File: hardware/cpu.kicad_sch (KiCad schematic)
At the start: 5 parts, among them U3 ESP32-C3-WROOM-02

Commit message: Update.
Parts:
- removed Conn_02x1: Conn_02x05_Odd_Even, Connector_PinHeader_2.54mm:PinHeader_2x05_P2.54mm_Vertical, symbol Connector_Generic:Conn_02x05_Odd_Even
- added J3: Conn_02x04_Odd_Even, Connector_PinHeader_2.54mm:PinHeader_2x04_P2.54mm_Vertical, symbol Connector_Generic:Conn_02x04_Odd_Even
- renumbered D3 to D4, R15 to R4, R6 to R5
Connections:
- net GND: now also J3.5 (Pin_5), J3.7 (Pin_7)
- net at U3.12 (IO21/TXD): now also J3.1 (Pin_1)
- net at U3.11 (IO20/RXD): now also J3.2 (Pin_2)
- net at U3.4 (IO5): now also J3.3 (Pin_3)
- net at U3.17 (IO1): now also J3.4 (Pin_4)
- net at U3.15 (IO3): now also J3.6 (Pin_6)
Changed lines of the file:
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@@
+	)
+	(junction
+		(at 36.83 58.42)
+		(diameter 0)
+		(color 0 0 0 0)
 	)
 	(junction
@@
 	(wire
 		(pts
-			(xy 34.29 58.42) (xy 36.83 58.42)
-		)
-		(stroke
-			(width 0)
-			(type default)
-		)
-	)
-	(wire
-		(pts
 			(xy 49.53 53.34) (xy 54.61 53.34)
 		)
@@
 	(wire
 		(pts
-			(xy 49.53 58.42) (xy 52.07 58.42)
-		)
-		(stroke
-			(width 0)
-			(type default)
-		)
-	)
-	(wire
-		(pts
-			(xy 52.07 63.5) (xy 95.25 63.5)
-		)
-		(stroke
-			(width 0)
-			(type default)
-		)
-	)
-	(wire
-		(pts
 			(xy 92.71 41.91) (xy 92.71 48.26)
 		)
@@
 	(wire
 		(pts
-			(xy 95.25 78.74) (xy 34.29 78.74)
-		)
-		(stroke
-			(width 0)
-			(type default)
-		)
-	)
-	(wire
-		(pts
-			(xy 34.29 78.74) (xy 34.29 58.42)
+			(xy 36.83 55.88) (xy 36.83 58.42)
 		)
 		(stroke
@@
 	(wire
 		(pts
-			(xy 95.25 71.12) (xy 33.02 71.12)
-		)
-		(stroke
-			(width 0)
-			(type default)
-		)
-	)
-	(wire
-		(pts
 			(xy 104.14 38.1) (xy 110.49 38.1)
 		)
@@
 	(wire
 		(pts
+			(xy 36.83 58.42) (xy 36.83 60.96)
+		)
+		(stroke
+			(width 0)
+			(type default)
+		)
+	)
+	(wire
+		(pts
 			(xy 76.2 38.1) (xy 104.14 38.1)
 		)
@@
 	(wire
 		(pts
-			(xy 33.02 71.12) (xy 33.02 55.88)
-		)
-		(stroke
-			(width 0)
-			(type default)
-		)
-	)
-	(wire
-		(pts
 			(xy 36.83 53.34) (xy 31.75 53.34)
 		)
@@
 		(pts
 			(xy 110.49 38.1) (xy 110.49 43.18)
-		)
-		(stroke
-			(width 0)
-			(type default)
-		)
-	)
-	(wire
-		(pts
-			(xy 52.07 63.5) (xy 52.07 58.42)
-		)
-		(stroke
-			(width 0)
-			(type default)
-		)
-	)
-	(wire
-		(pts
-			(xy 33.02 55.88) (xy 36.83 55.88)
 		)
 		(stroke
@@
 		(dnp no)
 		(fields_autoplaced yes)
-		(property "Reference" "R6"
+		(property "Reference" "R5"
 			(at 85.09 35.56 90)
 			(effects
@@
 			(project ""
 				(path "/90430e5f-7049-4de8-b92d-f897c4a89819/99bf9233-4f4b-4c20-a5a1-eeea9a6ff67a"
-					(reference "R6")
+					(reference "R5")
 					(unit 1)
 				)
@@
 	)
 	(symbol
-		(lib_id "Connector_Generic:Conn_02x05_Odd_Even")
-		(at 41.91 55.88 0)
+		(lib_id "Connector_Generic:Conn_02x04_Odd_Even")
+		(at 41.91 53.34 0)
 		(unit 1)
 		(exclude_from_sim no)
@@
 		(dnp no)
 		(fields_autoplaced yes)
-		(property "Reference" "Conn_02x1"
+		(property "Reference" "J3"
 			(at 43.18 44.45 0)
 			(effects
@@
 					(size 1.27 1.27)
 				)
-				(hide yes)
-			)
-		)
-		(property "Value" "Conn_02x05_Odd_Even"
+			)
+		)
+		(property "Value" "Conn_02x04_Odd_Even"
 			(at 43.18 46.99 0)
 			(effects
@@
 			)
 		)
-		(property "Footprint" "Connector_PinHeader_2.54mm:PinHeader_2x05_P2.54mm_Vertical"
-			(at 41.91 55.88 0)
+		(property "Footprint" "Connector_PinHeader_2.54mm:PinHeader_2x04_P2.54mm_Vertical"
+			(at 41.91 53.34 0)
 			(effects
 				(font
@@
 		)
 		(property "Datasheet" "~"
-			(at 41.91 55.88 0)
-			(effects
-				(font
-					(size 1.27 1.27)
-				)
-				(hide yes)
-			)
-		)
-		(property "Description" "Generic connector, double row, 02x05, odd/even pin numbering scheme (row 1 odd numbers, row 2 even numbers), script generated (kicad-library-utils/schlib/autogen/connector/)"
-			(at 41.91 55.88 0)
-			(effects
-				(font
-					(size 1.27 1.27)
-				)
-				(hide yes)
-			)
+			(at 41.91 53.34 0)
+			(effects
+				(font
+					(size 1.27 1.27)
+				)
+				(hide yes)
+			)
+		)
+		(property "Description" "Generic connector, double row, 02x04, odd/even pin numbering scheme (row 1 odd numbers, row 2 even numbers), script generated (kicad-library-utils/schlib/autogen/connector/)"
+			(at 41.91 53.34 0)
+			(effects
+				(font
+					(size 1.27 1.27)
+				)
+				(hide yes)
+			)
+		)
+		(pin "3"
+		)
+		(pin "8"
+		)
+		(pin "1"
 		)
 		(pin "5"
 		)
+		(pin "7"
+		)
+		(pin "2"
+		)
+		(pin "4"
+		)
 		(pin "6"
 		)
-		(pin "2"
-		)
-		(pin "7"
-		)
-		(pin "10"
-		)
-		(pin "9"
-		)
-		(pin "8"
-		)
-		(pin "4"
-		)
-		(pin "1"
-		)
-		(pin "3"
-		)
 		(instances
-			(project ""
+			(project "nixie_clock"
 				(path "/90430e5f-7049-4de8-b92d-f897c4a89819/99bf9233-4f4b-4c20-a5a1-eeea9a6ff67a"
-					(reference "Conn_02x1")
+					(reference "J3")
 					(unit 1)
 				)
@@
 		(on_board yes)
 		(dnp no)
-		(property "Reference" "D3"
+		(property "Reference" "D4"
 			(at 87.3125 46.99 0)
 			(effects
@@
 			(project ""
 				(path "/90430e5f-7049-4de8-b92d-f897c4a89819/99bf9233-4f4b-4c20-a5a1-eeea9a6ff67a"
-					(reference "D3")
+					(reference "D4")
 					(unit 1)
 				)
@@
 		(dnp no)
 		(fields_autoplaced yes)
-		(property "Reference" "R15"
+		(property "Reference" "R4"
 			(at 80.01 46.99 90)
 			(effects
@@
 			(project ""
 				(path "/90430e5f-7049-4de8-b92d-f897c4a89819/99bf9233-4f4b-4c20-a5a1-eeea9a6ff67a"
-					(reference "R15")
+					(reference "R4")
 					(unit 1)
 				)

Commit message: First routage.
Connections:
- net GND: no longer J3.5 (Pin_5), J3.7 (Pin_7)
- net at J3.1 (Pin_1): now also U3.11 (IO20/RXD); no longer U3.12 (IO21/TXD)
- net at J3.2 (Pin_2): now also U3.12 (IO21/TXD); no longer U3.11 (IO20/RXD)
- net at J3.3 (Pin_3): no longer U3.4 (IO5)
- net at J3.4 (Pin_4): no longer U3.17 (IO1)
- net at J3.6 (Pin_6): no longer U3.15 (IO3)
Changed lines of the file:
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@@
-	)
-	(junction
-		(at 36.83 58.42)
-		(diameter 0)
-		(color 0 0 0 0)
 	)
 	(junction
@@
 	(wire
 		(pts
-			(xy 53.34 60.96) (xy 95.25 60.96)
+			(xy 50.8 29.21) (xy 50.8 50.8)
 		)
 		(stroke
@@
 	(wire
 		(pts
-			(xy 49.53 53.34) (xy 54.61 53.34)
-		)
-		(stroke
-			(width 0)
-			(type default)
-		)
-	)
-	(wire
-		(pts
 			(xy 92.71 41.91) (xy 92.71 48.26)
 		)
@@
 	(wire
 		(pts
+			(xy 35.56 50.8) (xy 36.83 50.8)
+		)
+		(stroke
+			(width 0)
+			(type default)
+		)
+	)
+	(wire
+		(pts
 			(xy 87.63 81.28) (xy 95.25 81.28)
 		)
@@
 	(wire
 		(pts
-			(xy 53.34 55.88) (xy 53.34 60.96)
-		)
-		(stroke
-			(width 0)
-			(type default)
-		)
-	)
-	(wire
-		(pts
-			(xy 49.53 55.88) (xy 53.34 55.88)
-		)
-		(stroke
-			(width 0)
-			(type default)
-		)
-	)
-	(wire
-		(pts
-			(xy 36.83 29.21) (xy 36.83 50.8)
-		)
-		(stroke
-			(width 0)
-			(type default)
-		)
-	)
-	(wire
-		(pts
-			(xy 36.83 29.21) (xy 139.7 29.21)
+			(xy 35.56 30.48) (xy 138.43 30.48)
 		)
 		(stroke
@@
 	(wire
 		(pts
-			(xy 36.83 55.88) (xy 36.83 58.42)
-		)
-		(stroke
-			(width 0)
-			(type default)
-		)
-	)
-	(wire
-		(pts
 			(xy 87.63 68.58) (xy 95.25 68.58)
 		)
@@
 	(wire
 		(pts
+			(xy 50.8 29.21) (xy 139.7 29.21)
+		)
+		(stroke
+			(width 0)
+			(type default)
+		)
+	)
+	(wire
+		(pts
 			(xy 110.49 38.1) (xy 110.49 33.02)
 		)
@@
 	(wire
 		(pts
-			(xy 31.75 53.34) (xy 31.75 66.04)
-		)
-		(stroke
-			(width 0)
-			(type default)
-		)
-	)
-	(wire
-		(pts
 			(xy 66.04 50.8) (xy 66.04 53.34)
 		)
@@
 	(wire
 		(pts
-			(xy 31.75 66.04) (xy 95.25 66.04)
-		)
-		(stroke
-			(width 0)
-			(type default)
-		)
-	)
-	(wire
-		(pts
 			(xy 110.49 88.9) (xy 110.49 91.44)
 		)
@@
 	(wire
 		(pts
+			(xy 35.56 30.48) (xy 35.56 50.8)
+		)
+		(stroke
+			(width 0)
+			(type default)
+		)
+	)
+	(wire
+		(pts
+			(xy 49.53 50.8) (xy 50.8 50.8)
+		)
+		(stroke
+			(width 0)
+			(type default)
+		)
+	)
+	(wire
+		(pts
 			(xy 104.14 38.1) (xy 110.49 38.1)
 		)
@@
 	(wire
 		(pts
-			(xy 54.61 55.88) (xy 95.25 55.88)
-		)
-		(stroke
-			(width 0)
-			(type default)
-		)
-	)
-	(wire
-		(pts
-			(xy 35.56 60.96) (xy 36.83 60.96)
-		)
-		(stroke
-			(width 0)
-			(type default)
-		)
-	)
-	(wire
-		(pts
-			(xy 36.83 58.42) (xy 36.83 60.96)
-		)
-		(stroke
-			(width 0)
-			(type default)
-		)
-	)
-	(wire
-		(pts
 			(xy 76.2 38.1) (xy 104.14 38.1)
 		)
@@
 	(wire
 		(pts
-			(xy 36.83 53.34) (xy 31.75 53.34)
-		)
-		(stroke
-			(width 0)
-			(type default)
-		)
-	)
-	(wire
-		(pts
 			(xy 87.63 83.82) (xy 95.25 83.82)
 		)
@@
 	(wire
 		(pts
-			(xy 49.53 30.48) (xy 138.43 30.48)
-		)
-		(stroke
-			(width 0)
-			(type default)
-		)
-	)
-	(wire
-		(pts
 			(xy 92.71 53.34) (xy 95.25 53.34)
 		)
@@
 		(pts
 			(xy 87.63 76.2) (xy 95.25 76.2)
-		)
-		(stroke
-			(width 0)
-			(type default)
-		)
-	)
-	(wire
-		(pts
-			(xy 49.53 30.48) (xy 49.53 50.8)
-		)
-		(stroke
-			(width 0)
-			(type default)
-		)
-	)
-	(wire
-		(pts
-			(xy 54.61 53.34) (xy 54.61 55.88)
 		)
 		(stroke
@@
 		(effects
 			(font
-				(size 1.27 1.27)
-			)
-			(justify right)
-		)
-	)
-	(hierarchical_label "GND"
-		(shape input)
-		(at 35.56 60.96 180)
-		(effects
-			(font

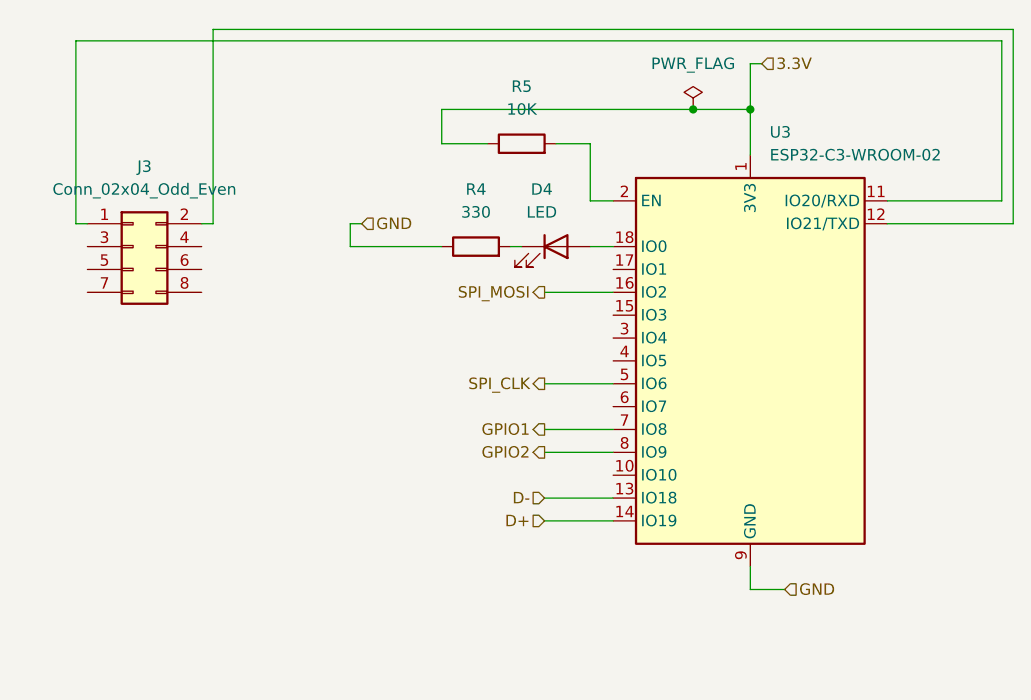
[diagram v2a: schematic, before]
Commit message: Add buttons.
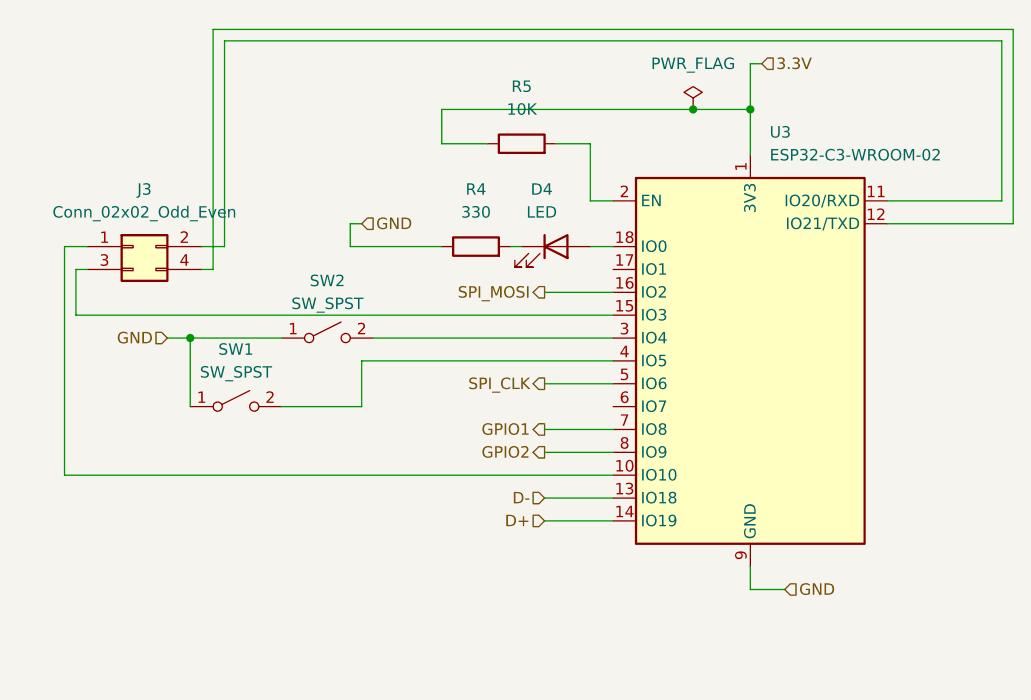
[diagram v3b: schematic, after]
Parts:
- added SW1, SW2: SW_SPST, Button_Switch_THT:SW_Tactile_SPST_Angled_PTS645Vx58-2LFS, symbol Switch:SW_SPST
- J3: value Conn_02x04_Odd_Even -> Conn_02x02_Odd_Even; footprint Connector_PinHeader_2.54mm:PinHeader_2x04_P2.54mm_Vertical -> Connector_PinHeader_2.54mm:PinHeader_2x02_P2.54mm_Vertical_SMD; symbol Connector_Generic:Conn_02x04_Odd_Even -> Connector_Generic:Conn_02x02_Odd_Even
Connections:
- net GND: now also SW1.1 (A), SW2.1 (A)
- net at J3.1 (Pin_1): now also U3.10 (IO10); no longer U3.11 (IO20/RXD)
- net at J3.2 (Pin_2): now also U3.11 (IO20/RXD); no longer U3.12 (IO21/TXD)
- net at J3.3 (Pin_3): now also U3.15 (IO3)
- net at J3.4 (Pin_4): now also U3.12 (IO21/TXD)
- net at U3.3 (IO4): now also SW2.2 (B)
- net at U3.4 (IO5): now also SW1.2 (B)

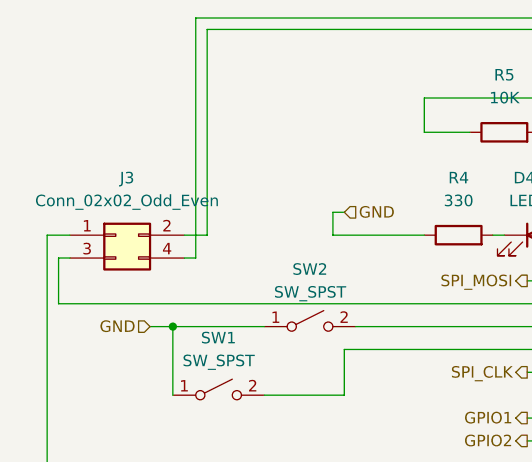
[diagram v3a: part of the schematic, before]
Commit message: Add HT psu.
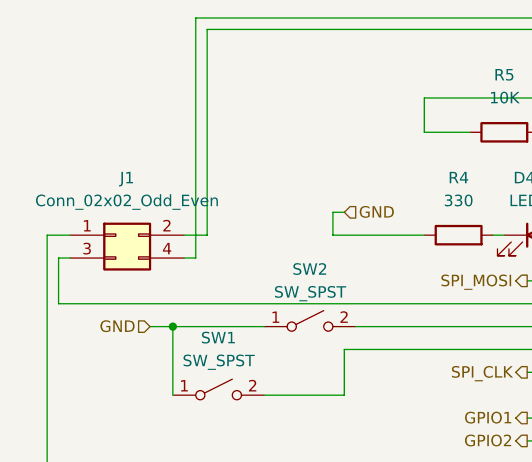
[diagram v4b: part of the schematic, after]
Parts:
- renumbered J3 to J1
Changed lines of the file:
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@@
 		(dnp no)
 		(fields_autoplaced yes)
-		(property "Reference" "J3"
+		(property "Reference" "J1"
 			(at 43.18 46.99 0)
 			(effects
@@
 			(project "nixie_clock"
 				(path "/90430e5f-7049-4de8-b92d-f897c4a89819/99bf9233-4f4b-4c20-a5a1-eeea9a6ff67a"
-					(reference "J3")
+					(reference "J1")
 					(unit 1)
 				)

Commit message: Update.
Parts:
- added R21, R22: 10k, Resistor_SMD:R_1206_3216Metric, symbol Device:R
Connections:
- net at SW2.2 (B): now also R21.1; no longer U3.3 (IO4)
- net at SW1.2 (B): now also R22.1; no longer U3.4 (IO5)
- new net: R22.2, U3.4 (IO5)
- new net: R21.2, U3.3 (IO4)
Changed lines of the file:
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@@
+	(wire
+		(pts
+			(xy 68.58 63.5) (xy 80.01 63.5)
+		)
+		(stroke
+			(width 0)
+			(type default)
+		)
+	)
 	(wire
 		(pts
@@
 	(wire
 		(pts
+			(xy 78.74 66.04) (xy 95.25 66.04)
+		)
+		(stroke
+			(width 0)
+			(type default)
+		)
+	)
+	(wire
+		(pts
 			(xy 92.71 41.91) (xy 92.71 48.26)
 		)
@@
 	(wire
 		(pts
+			(xy 87.63 63.5) (xy 95.25 63.5)
+		)
+		(stroke
+			(width 0)
+			(type default)
+		)
+	)
+	(wire
+		(pts
 			(xy 85.09 53.34) (xy 83.82 53.34)
 		)
@@
 	(wire
 		(pts
-			(xy 67.31 66.04) (xy 95.25 66.04)
-		)
-		(stroke
-			(width 0)
-			(type default)
-		)
-	)
-	(wire
-		(pts
 			(xy 67.31 71.12) (xy 67.31 66.04)
 		)
@@
 	(wire
 		(pts
-			(xy 68.58 63.5) (xy 95.25 63.5)
-		)
-		(stroke
-			(width 0)
-			(type default)
-		)
-	)
-	(wire
-		(pts
 			(xy 76.2 38.1) (xy 104.14 38.1)
 		)
@@
 		(pts
 			(xy 88.9 41.91) (xy 92.71 41.91)
+		)
+		(stroke
+			(width 0)
+			(type default)
+		)
+	)
+	(wire
+		(pts
+			(xy 67.31 66.04) (xy 71.12 66.04)
 		)
 		(stroke
@@
 				(path "/90430e5f-7049-4de8-b92d-f897c4a89819/99bf9233-4f4b-4c20-a5a1-eeea9a6ff67a"
 					(reference "SW1")
+					(unit 1)
+				)
+			)
+		)
+	)
+	(symbol
+		(lib_id "Device:R")
+		(at 74.93 66.04 90)
+		(unit 1)
+		(exclude_from_sim no)
+		(in_bom yes)
+		(on_board yes)
+		(dnp no)
+		(fields_autoplaced yes)
+		(property "Reference" "R22"
+			(at 74.93 59.69 90)
+			(effects
+				(font
+					(size 1.27 1.27)
+				)
+			)
+		)
+		(property "Value" "10k"
+			(at 74.93 62.23 90)
+			(effects
+				(font
+					(size 1.27 1.27)
+				)
+			)
+		)
+		(property "Footprint" "Resistor_SMD:R_1206_3216Metric"
+			(at 74.93 67.818 90)
+			(effects
+				(font
+					(size 1.27 1.27)
+				)
+				(hide yes)
+			)
+		)
+		(property "Datasheet" "~"
+			(at 74.93 66.04 0)
+			(effects
+				(font
+					(size 1.27 1.27)
+				)
+				(hide yes)
+			)
+		)
+		(property "Description" "Resistor"
+			(at 74.93 66.04 0)
+			(effects
+				(font
+					(size 1.27 1.27)
+				)
+				(hide yes)
+			)
+		)
+		(pin "1"
+		)
+		(pin "2"
+		)
+		(instances
+			(project "nixie_clock"
+				(path "/90430e5f-7049-4de8-b92d-f897c4a89819/99bf9233-4f4b-4c20-a5a1-eeea9a6ff67a"
+					(reference "R22")
 					(unit 1)
 				)
@@
 					(unit 1)
 				)
+			)
+		)
+	)
+	(symbol
+		(lib_id "Device:R")
+		(at 83.82 63.5 90)
+		(unit 1)
+		(exclude_from_sim no)
+		(in_bom yes)
+		(on_board yes)
+		(dnp no)
+		(fields_autoplaced yes)
+		(property "Reference" "R21"
+			(at 83.82 57.15 90)
+			(effects
+				(font
+					(size 1.27 1.27)
+				)
+			)
+		)
+		(property "Value" "10k"
+			(at 83.82 59.69 90)
+			(effects
+				(font
+					(size 1.27 1.27)
+				)
+			)
+		)
+		(property "Footprint" "Resistor_SMD:R_1206_3216Metric"
+			(at 83.82 65.278 90)
+			(effects
+				(font
+					(size 1.27 1.27)
+				)
+				(hide yes)
+			)
+		)
+		(property "Datasheet" "~"
+			(at 83.82 63.5 0)
+			(effects
+				(font
+					(size 1.27 1.27)
+				)
+				(hide yes)
+			)
+		)
+		(property "Description" "Resistor"
+			(at 83.82 63.5 0)
+			(effects
+				(font
+					(size 1.27 1.27)
+				)
+				(hide yes)
+			)
+		)
+		(pin "1"
+		)
+		(pin "2"
+		)
+		(instances
+			(project "nixie_clock"
+				(path "/90430e5f-7049-4de8-b92d-f897c4a89819/99bf9233-4f4b-4c20-a5a1-eeea9a6ff67a"
+					(reference "R21")
+					(unit 1)
+				)

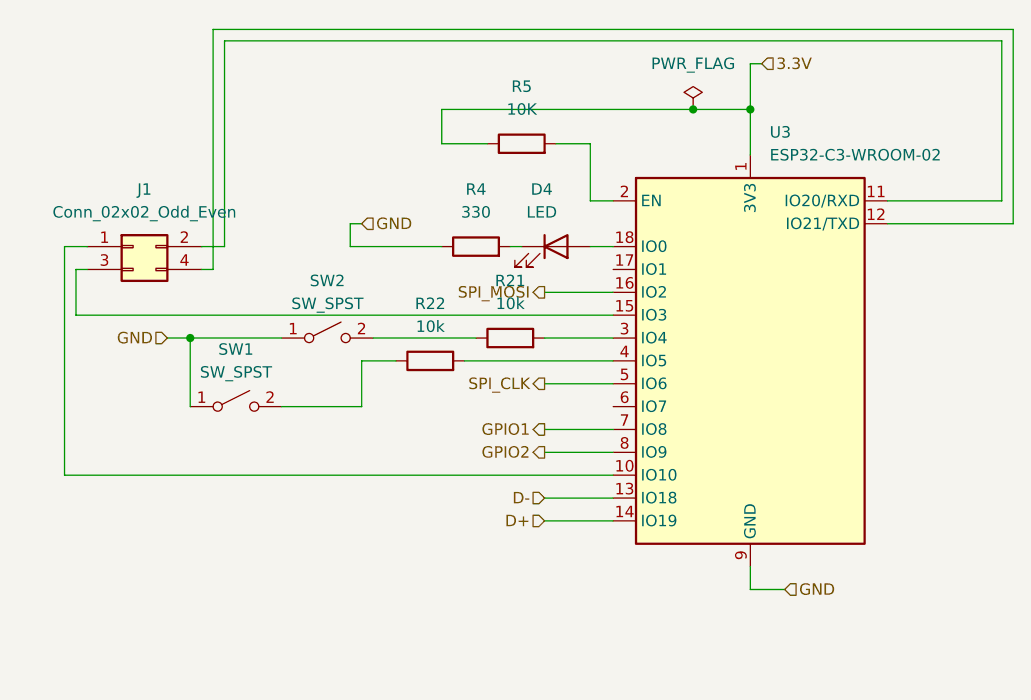
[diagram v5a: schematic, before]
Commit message: Add decoupling capacitor for MCU. Fix circuit to avoid VCC being between capacitor and power pad.
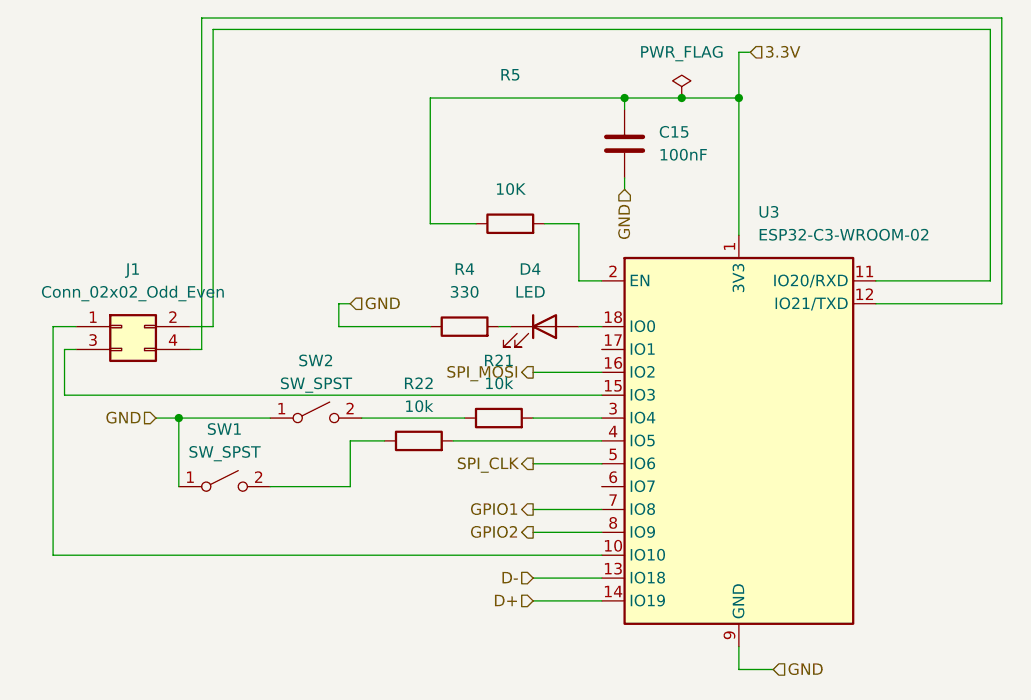
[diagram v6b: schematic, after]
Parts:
- added C15: 100nF, Capacitor_SMD:C_1206_3216Metric, symbol Device:C
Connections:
- net 3.3V: now also C15.1
- net GND: now also C15.2
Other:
- moved on the sheet: D4, J1, R21, R22, R4, R5, SW1, SW2, U3

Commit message: C15, C13, C9  changed to 805 form factor. Removed tracks under capacitors.
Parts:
- C15: footprint Capacitor_SMD:C_1206_3216Metric -> Resistor_SMD:R_0805_2012Metric
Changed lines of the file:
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@@
 			)
 		)
-		(property "Footprint" "Capacitor_SMD:C_1206_3216Metric"
+		(property "Footprint" "Resistor_SMD:R_0805_2012Metric"
 			(at 97.4852 45.72 0)
 			(effects

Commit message: Update D4 and R4 to 805 size.
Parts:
- D4: footprint LED_SMD:LED_1206_3216Metric -> LED_SMD:LED_0805_2012Metric
- R4: footprint Resistor_SMD:R_1206_3216Metric -> Resistor_SMD:R_0805_2012Metric
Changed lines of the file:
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@@
 			)
 		)
-		(property "Footprint" "LED_SMD:LED_1206_3216Metric"
+		(property "Footprint" "LED_SMD:LED_0805_2012Metric"
 			(at 87.63 62.23 0)
 			(effects
@@
 			)
 		)
-		(property "Footprint" "Resistor_SMD:R_1206_3216Metric"
+		(property "Footprint" "Resistor_SMD:R_0805_2012Metric"
 			(at 78.74 64.008 90)
 			(effects
